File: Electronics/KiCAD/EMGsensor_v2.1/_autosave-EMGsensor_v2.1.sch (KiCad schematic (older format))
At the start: 37 parts, among them J1 Conn_01x03_Male, J2 Conn_01x02_Male, J3 Conn_01x03_Male, J4 SHIFT, J5 NO_SHIFT, U1 OPA4234P, U2 AD623, U3 OPA4234P

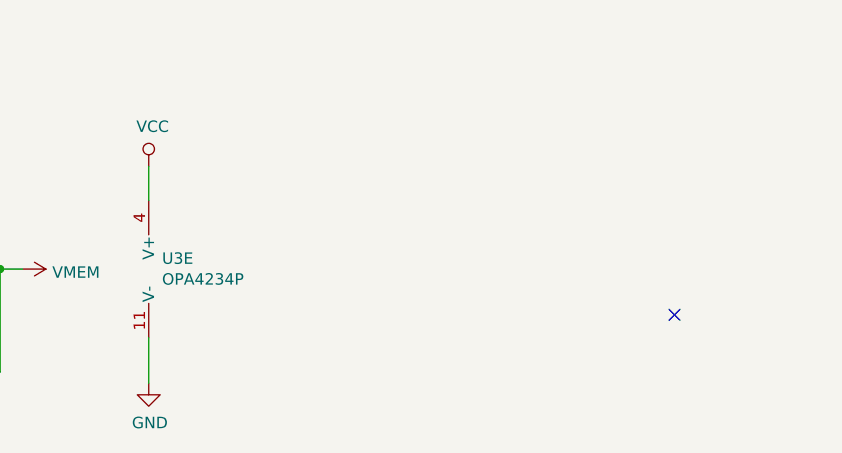
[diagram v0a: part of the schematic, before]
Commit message: Schematic finish, add gitignore
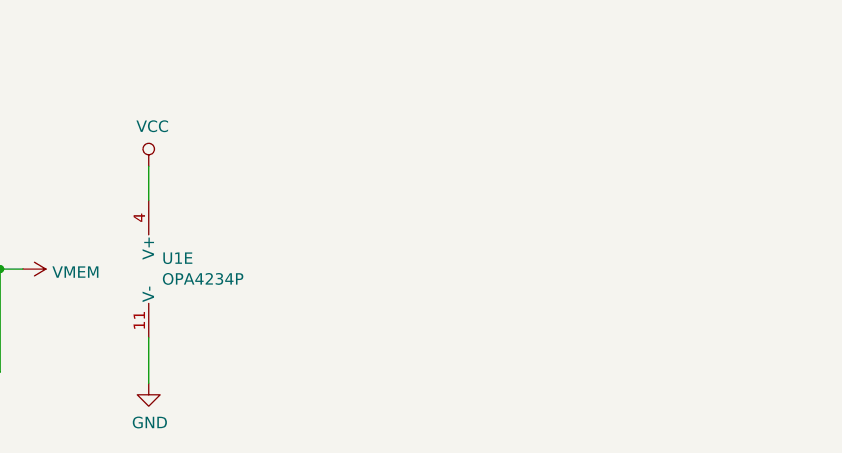
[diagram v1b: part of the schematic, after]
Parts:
- renumbered U3 to U1
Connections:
- no-connect marks 2 -> 1
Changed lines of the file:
@@
 	3900 4700 3750 4700
 $Comp
-L Amplifier_Operational:OPA4376 U3
+L Amplifier_Operational:OPA4376 U1
 U 5 1 5D0433E8
 P 4650 4700
-F 0 "U3" H 4608 4746 50  0000 L CNN
+F 0 "U1" H 4608 4746 50  0000 L CNN
 F 1 "OPA4234P" H 4608 4655 50  0000 L CNN
 F 2 "Package_DIP:DIP-14_W10.16mm_LongPads" H 4600 4800 50  0001 C CNN
@@
 	850  4900 850  5000
 NoConn ~ 9550 1850
-NoConn ~ 6850 4900
 $Comp
 L Amplifier_Operational:OPA4376 U1
